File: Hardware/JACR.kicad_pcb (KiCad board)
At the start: 2 copper layers, 100 x 100 mm, 44 parts, among them J1 Barrel_Jack_Switch, J2 JACR CARTRIDGE SLOT, J3 EXP1, J4 EXP2, M1 MountingHole_2.2mm_M2_Pad, M2 MountingHole_2.2mm_M2_Pad, M3 MountingHole_2.2mm_M2_Pad, M4 MountingHole_2.2mm_M2_Pad, Q1 BSS138, Q2 BSS138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

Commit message: Wrong Resistor values for the power regulator circuit
Not sure where I got the old values but rereading the data sheet and testing is key to not overvolt anything
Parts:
- added REF**: JACR_LOGO, DiplomaticEntertainment:JACR_LOGO, F.Cu at (134.5, 135.1)
- R1: value 73.2kΩ -> 54.9kΩ
- R3: value 45.3kΩ -> 33.2kΩ
- RTCBATT1: value Battery_Cell CR1216 -> Battery_Cell
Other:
- board text added: "Just Another Cartridge Reader (C) 2025 Diplomatic Entertainment, LLC. Creative Commons Attribution 4.0 International (CC BY 4.0)"
- board text removed: "Just Another Cartridge Reader (C) 2025 Diplomatic Entertainment, LLC."

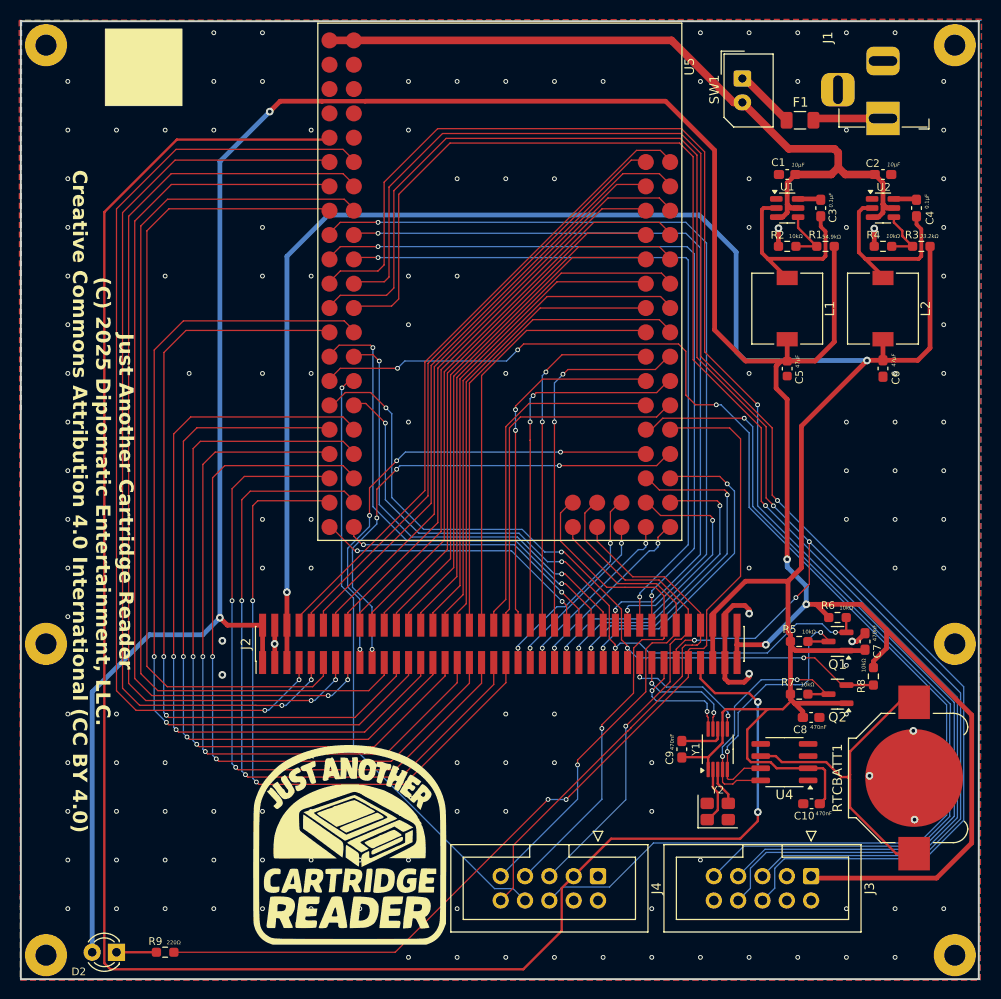
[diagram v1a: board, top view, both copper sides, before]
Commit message: Reroute traces going to the display connectors
Added logos as well
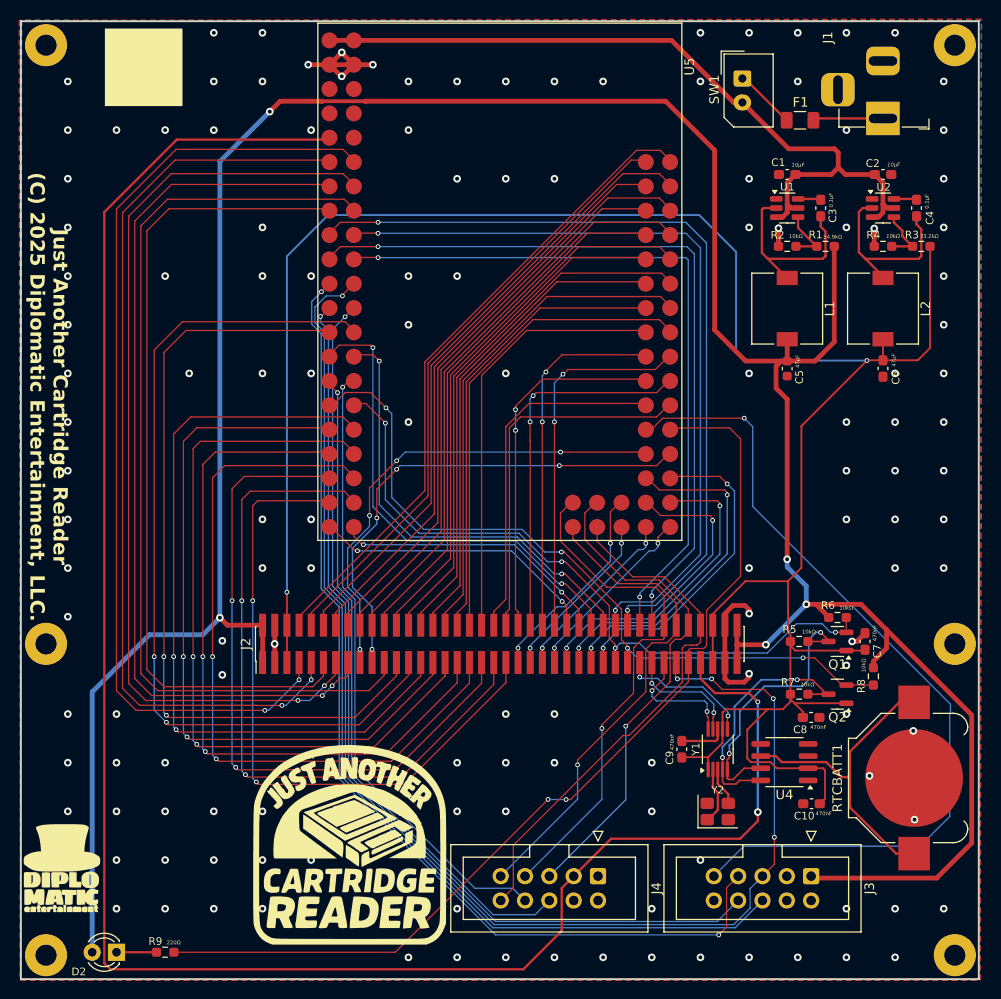
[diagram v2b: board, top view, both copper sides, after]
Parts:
- added REF**: DELogo_Small, DiplomaticEntertainment:DELogo_Small, F.Cu at (104.0, 137.5)
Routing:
- net D19: track 145.5 -> 69.3 mm, vias 3 -> 1
- net D12: track 157.6 -> 98.2 mm
- net D11: track 157.2 -> 107.0 mm, vias 1 -> 2
- net D10: track 155.7 -> 106.9 mm
- net D13: track 178.7 -> 135.4 mm, vias 4 -> 5
- net GND: track 27.8 -> 41.7 mm, vias 144 -> 139
- net D18: track 64.2 -> 65.3 mm
- net +3V3: track 242.2 -> 241.4 mm
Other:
- board text added: "Just Another Cartridge Reader (C) 2025 Diplomatic Entertainment, LLC."
- board text removed: "Just Another Cartridge Reader (C) 2025 Diplomatic Entertainment, LLC. Creative Commons Attribution 4.0 International (CC BY 4.0)"

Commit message: Modified power circuitry
Changed inductor to a more readily available part
Simplified 3.3V rail to linear regulator part
After some testing, reduced fuse value, the whole unit barely hits 1 amp, might be higher during dumping
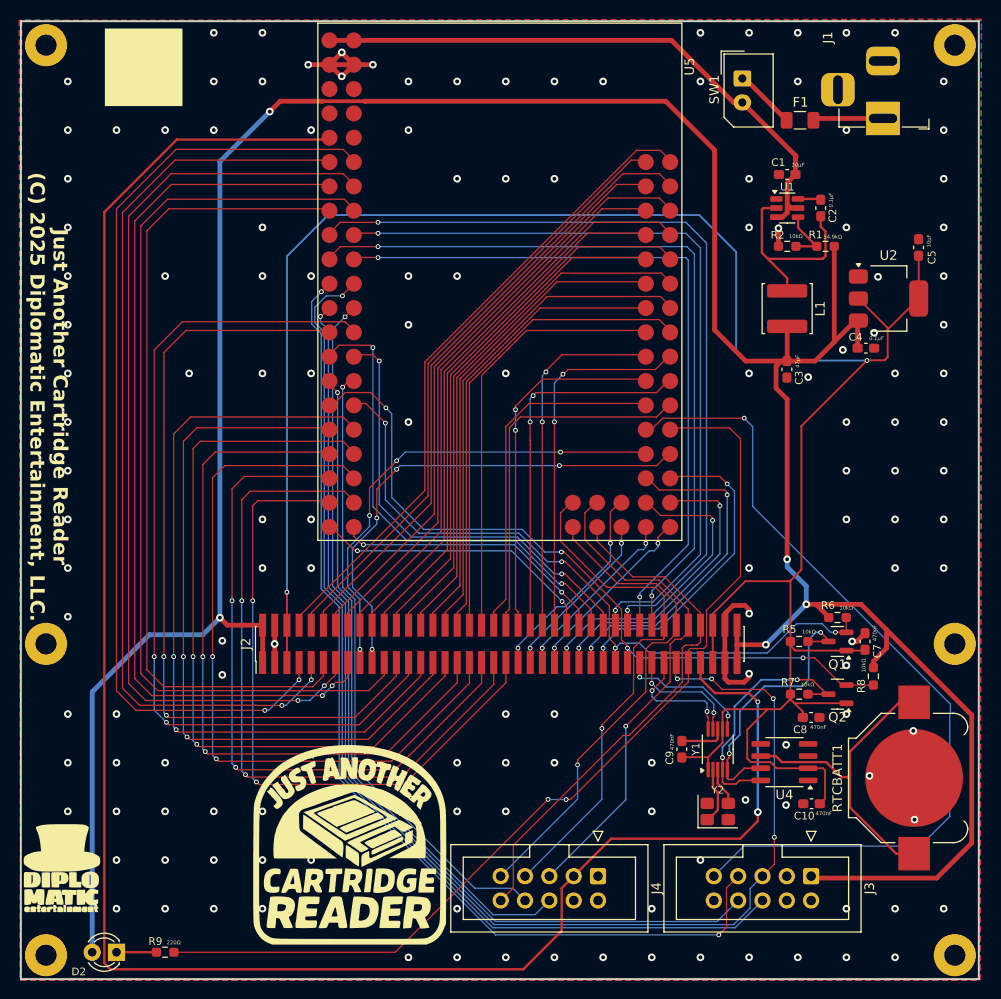
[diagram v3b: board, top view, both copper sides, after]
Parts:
- removed the C5 at (180.0, 86.3)
- removed C6: 47µF, Capacitor_SMD:C_0603_1608Metric_Pad1.08x0.95mm_HandSolder
- removed L2: 3.3µH, Generic:mps_mag_4600_smt_a
- removed R3: 33.2kΩ, Resistor_SMD:R_0603_1608Metric_Pad0.98x0.95mm_HandSolder
- removed R4: 10kΩ, Resistor_SMD:R_0603_1608Metric_Pad0.98x0.95mm_HandSolder
- added C3: 47µF, Capacitor_SMD:C_0603_1608Metric_Pad1.08x0.95mm_HandSolder, F.Cu at (180.0, 86.3)
- C4: renamed from C2; value 10µF -> 0.1µF
- C5: renamed from C4; value 0.1µF -> 10µF
- F1: value 2.5A -> 1A
- L1: footprint Generic:mps_mag_4600_smt_a -> Inductor_SMD:L_APV_ANR5040
- U2: value TPS563200 -> LD1117S33; footprint Package_TO_SOT_SMD:SOT-23-6 -> Package_TO_SOT_SMD:SOT-223-3_TabPin2
- moved C4 18.2 mm to (188.2, 84.1)
- moved U2 9.47 mm to (190.6, 79.0)
- moved C5 4.13 mm to (193.7, 73.6)
- renumbered C3 to C2
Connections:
- C4 pad 1: VCC -> +5V
- C5 pad 1: Net-(U2-SW) -> +3V3
- C5 pad 2: Net-(U2-VBST) -> GND
- U2 pad 2: Net-(U2-SW) -> +3V3
- U2 pad 3: VCC -> +5V
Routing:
- net VCC: track 82.3 -> 62.6 mm
- net Net-(U2-SW): track 19.6 -> 0.00 mm
- net +5V: track 302.1 -> 309.8 mm
- net Net-(U2-VFB): track 6.03 -> 0.00 mm
- net Net-(U2-VBST): track 2.28 -> 0.00 mm
- net GND: track 41.7 -> 39.9 mm, vias 139 -> 145
- net Net-(U1-SW): track 20.3 -> 21.6 mm
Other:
- board text added: "47µF"

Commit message: Widen 3.3V rail traces
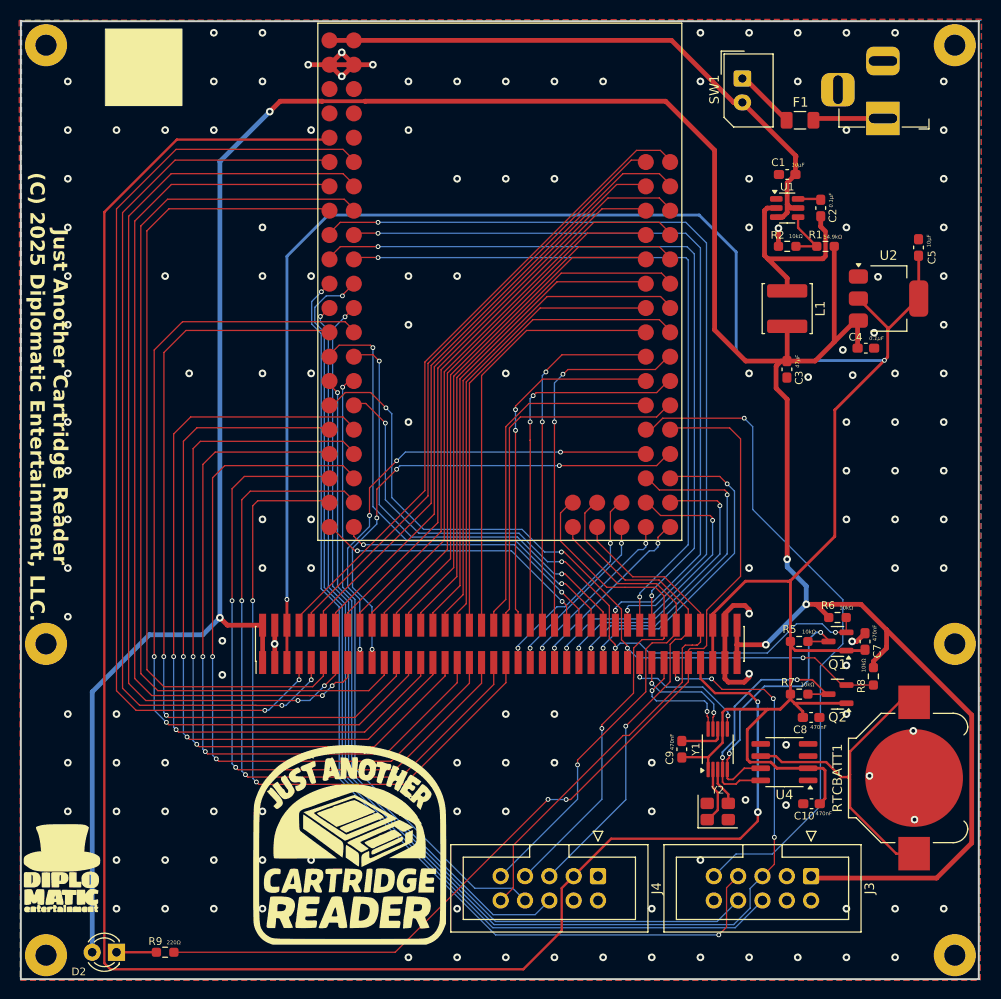
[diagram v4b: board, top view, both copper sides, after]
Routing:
- net D39: track 88.4 -> 70.6 mm
- net +3V3: track 241.4 -> 242.3 mm
- net GND: vias 145 -> 146

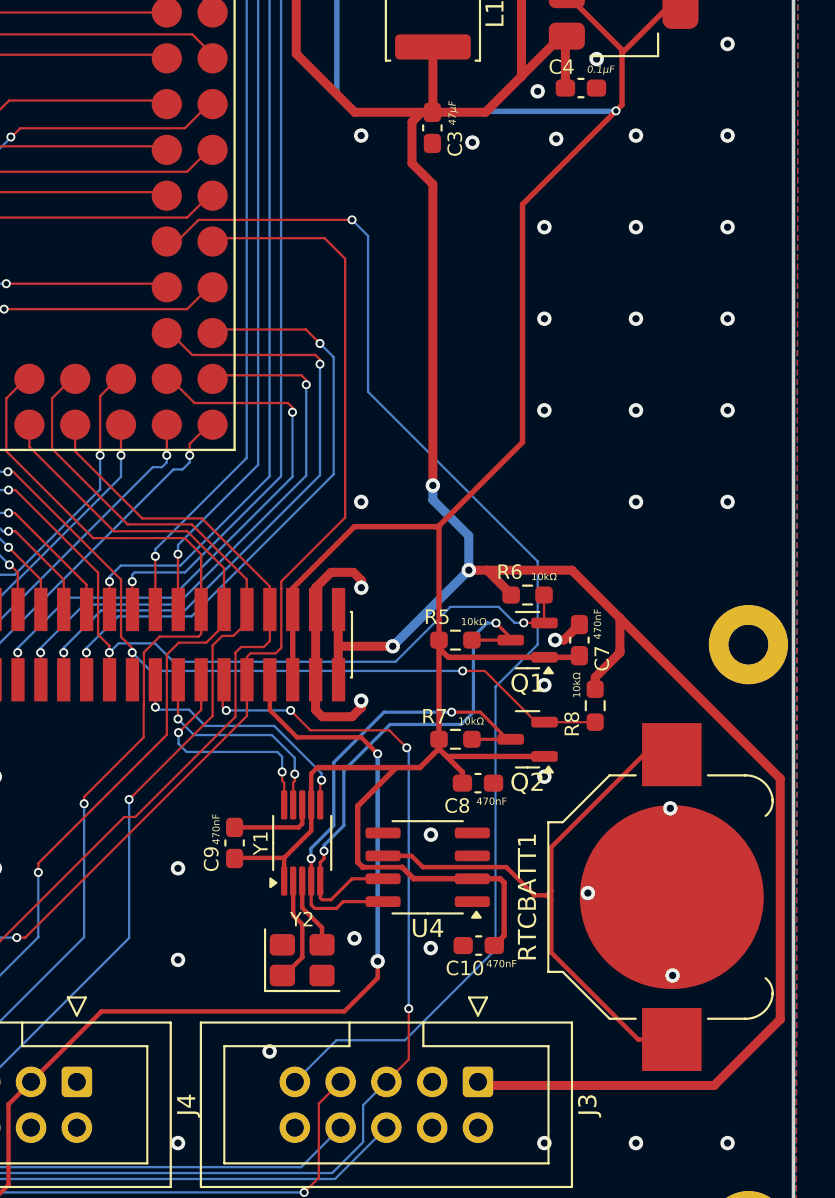
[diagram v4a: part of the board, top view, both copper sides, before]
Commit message: Modified Clock Gnerator/RTC Circuit
I believe putting the RTC I2C lines behind the transistors and pullups is causing problems with it not registering as present all the time. It may also be interfering with the Clock Generator.
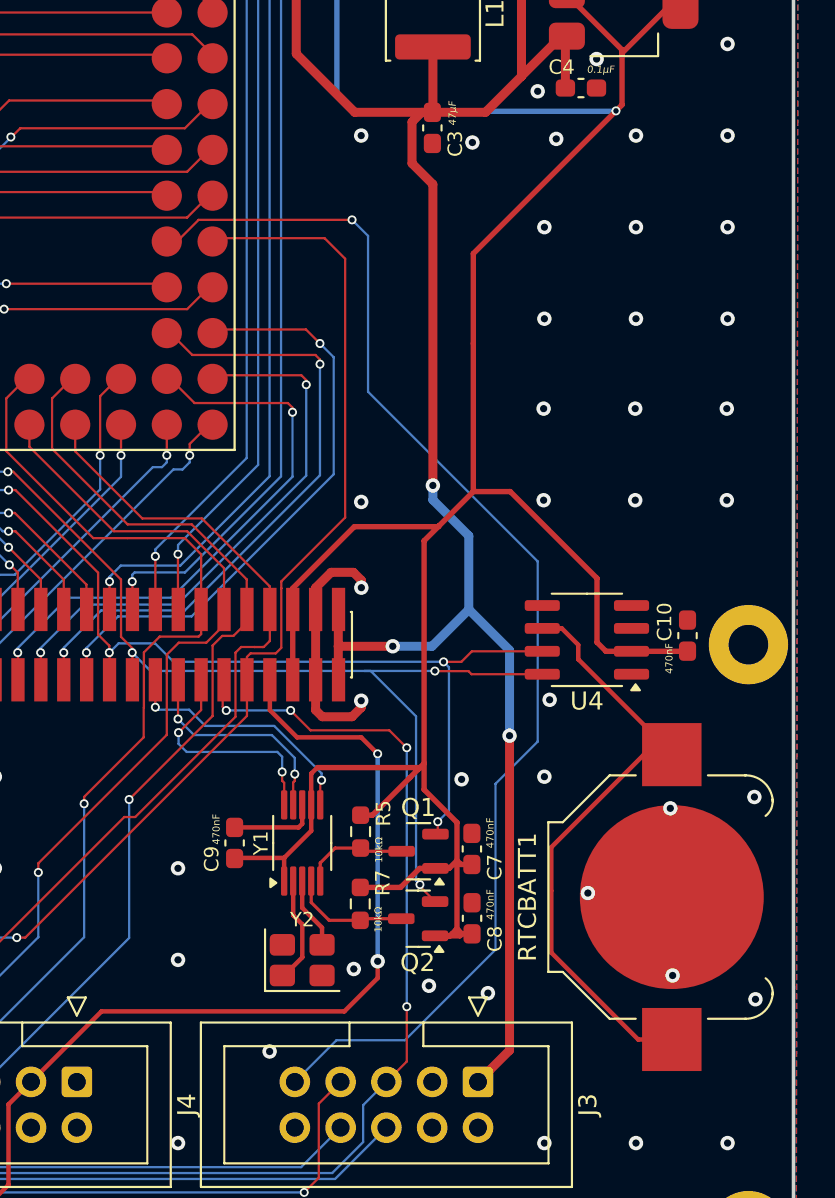
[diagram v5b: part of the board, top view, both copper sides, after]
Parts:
- removed R6, R8: 10kΩ, Resistor_SMD:R_0603_1608Metric_Pad0.98x0.95mm_HandSolder
- U1: value TPS563200 -> TPS562200
- moved C10 20.7 mm to (194.1, 114.5), turned to 90 degrees
- moved U4 15.4 mm to (188.5, 114.7)
- moved Q1 13.2 mm to (179.2, 126.5)
- moved C7 13.0 mm to (182.2, 126.3)
- moved R5 11.9 mm to (176.0, 125.4), turned to -90 degrees
- moved Q2 11.7 mm to (179.2, 130.2)
- moved R7 10.5 mm to (176.0, 129.4), turned to -90 degrees
- moved C8 7.50 mm to (182.2, 130.2), turned to 90 degrees
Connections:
- C10 pad 1: +3V3 -> +5V
- U4 pad 2: +3V3 -> +5V
- U4 pad 7: /SDA -> D20
- U4 pad 8: /SCL -> D21
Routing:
- net +5V: track 309.8 -> 278.8 mm
- net /SDA: track 29.3 -> 5.93 mm, vias 2 -> 0
- net /SCL: track 26.5 -> 6.63 mm, vias 2 -> 0
- net D21: track 78.6 -> 89.1 mm, vias 4 -> 5
- net +3V3: track 242.3 -> 249.8 mm
- net D20: track 74.3 -> 81.2 mm, vias 4 -> 5
- net GND: track 39.9 -> 38.1 mm, vias 146 -> 149

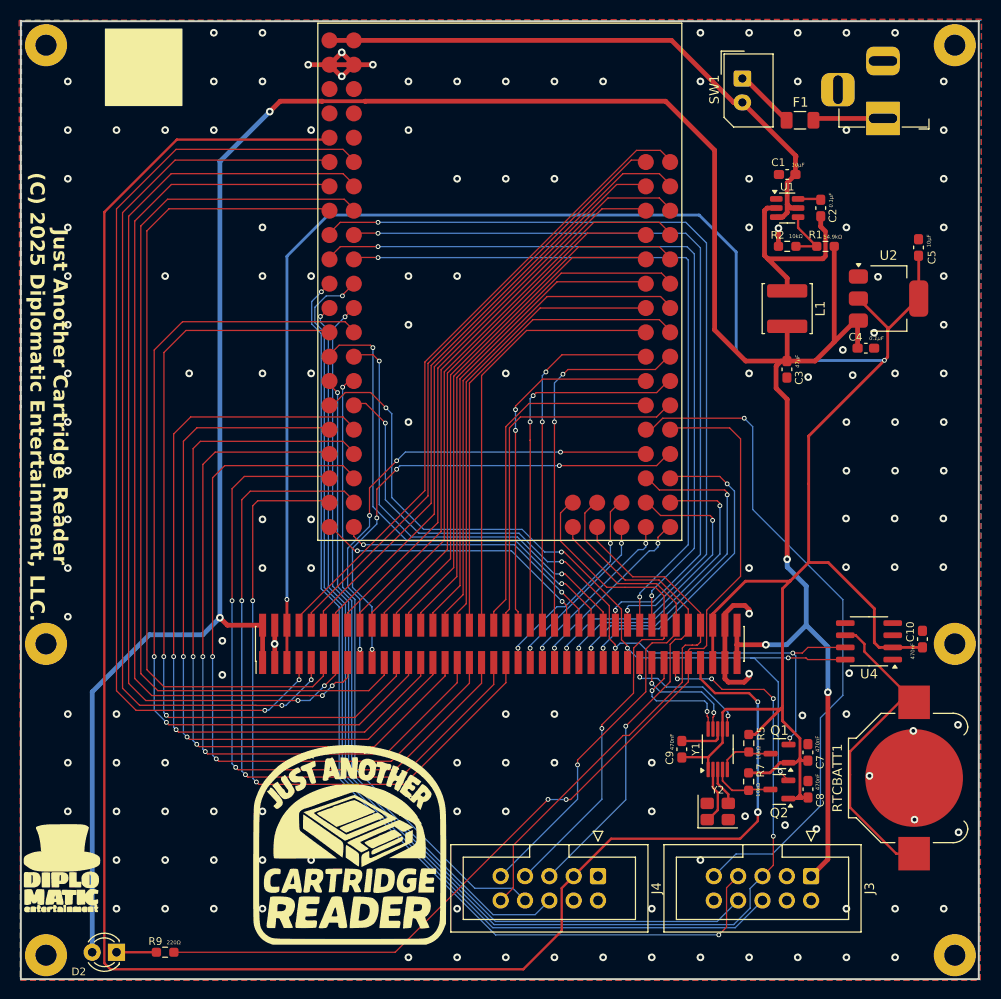
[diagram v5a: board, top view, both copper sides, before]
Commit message: Changing the Mega2560 footprint back to through-hole
Making it SMD seems to have provided no benefits and may have actually caused issues regarding data transfer.
Currently no successful dump of any cartridge has occurred.
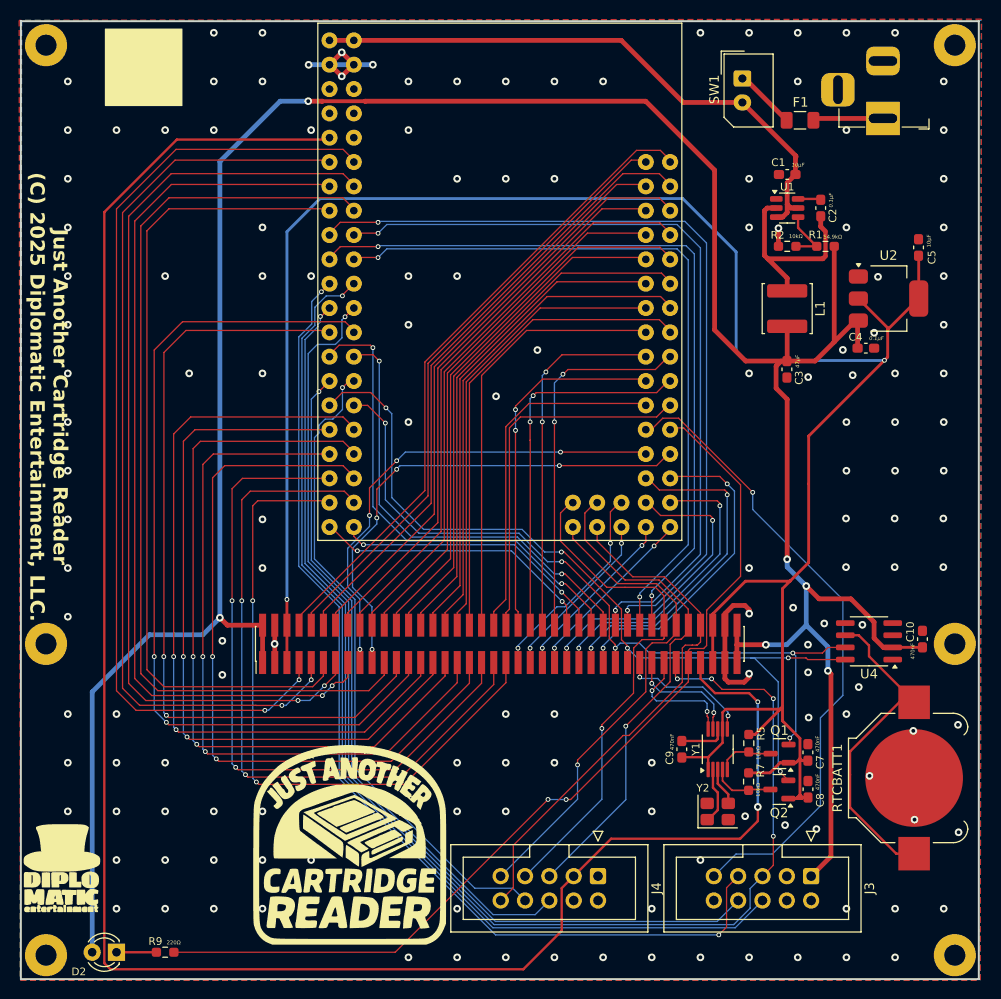
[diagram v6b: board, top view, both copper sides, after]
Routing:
- net +5V: track 278.8 -> 293.6 mm, vias 5 -> 6
- net +3V3: track 249.8 -> 235.8 mm
- net D39: track 70.6 -> 66.6 mm
- net D12: track 98.2 -> 101.4 mm
- net D18: track 65.3 -> 68.3 mm
- net D38: track 101.7 -> 98.9 mm
- net D19: track 69.3 -> 70.8 mm
- net D13: track 135.3 -> 136.6 mm
- net D11: track 107.0 -> 108.1 mm
- net D10: track 106.9 -> 108.1 mm
- net D8: track 75.2 -> 76.0 mm
- net D6: track 81.8 -> 82.6 mm
- net GND: track 38.1 -> 38.2 mm, vias 149 -> 151
